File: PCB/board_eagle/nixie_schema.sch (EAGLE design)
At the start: 103 parts, among them J2 RTC_CONSMD, J4 RTC_CONTHT, P1 100k, Q1 BC856B, Q2 IRF740S, T1 PHOTO_TRANS, U2 MC7940N, Y1 ECS-.327-7-34B

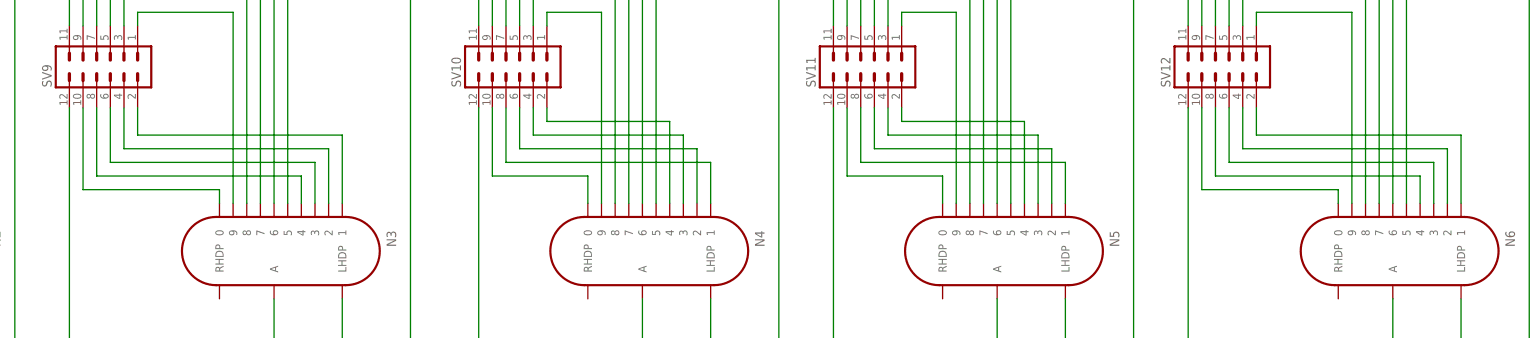
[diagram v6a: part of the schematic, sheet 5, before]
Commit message: Some more tob board routing
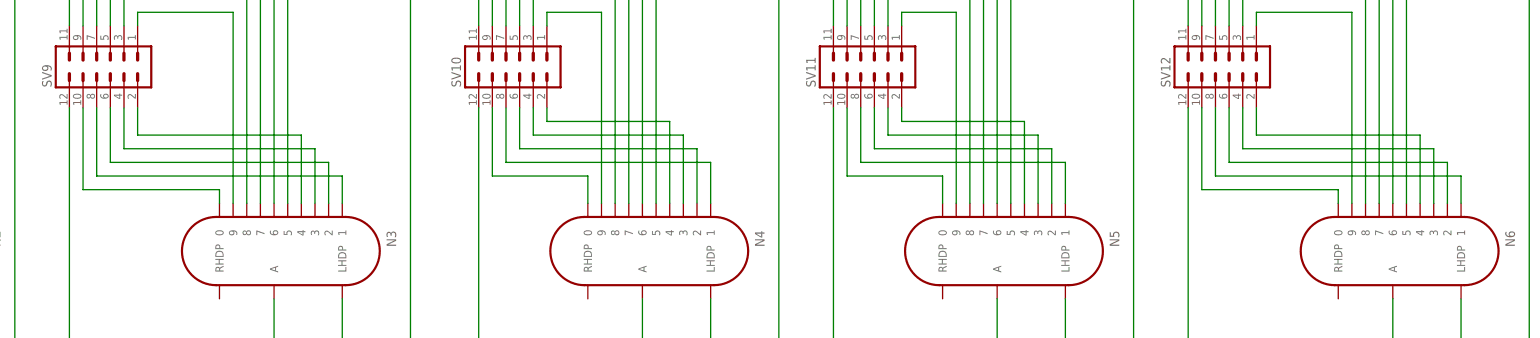
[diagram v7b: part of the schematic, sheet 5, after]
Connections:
- net N$52: now also N3.1; no longer N3.4
- net N$53: now also N3.2; no longer N3.3
- net N$54: now also N3.3; no longer N3.2
- net N$55: now also N3.4; no longer N3.1
- net N$81: now also N6.1; no longer N6.4
- net N$82: now also N6.2; no longer N6.3
- net N$83: now also N6.3; no longer N6.2
- net N$84: now also N6.4; no longer N6.1
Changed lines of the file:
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@@
 <net name="N$52" class="0">
 <segment>
+<pinref part="SV9" gate="1" pin="8"/>
+<wire x1="180.34" y1="25.4" x2="134.62" y2="25.4" width="0.1524" layer="91"/>
+<wire x1="134.62" y1="25.4" x2="134.62" y2="38.1" width="0.1524" layer="91"/>
+<pinref part="N3" gate="G$1" pin="1"/>
+<wire x1="180.34" y1="25.4" x2="180.34" y2="20.32" width="0.1524" layer="91"/>
+</segment>
+</net>
+<net name="N$53" class="0">
+<segment>
+<pinref part="SV9" gate="1" pin="6"/>
+<wire x1="137.16" y1="27.94" x2="137.16" y2="38.1" width="0.1524" layer="91"/>
+<pinref part="N3" gate="G$1" pin="2"/>
+<wire x1="137.16" y1="27.94" x2="177.8" y2="27.94" width="0.1524" layer="91"/>
+<wire x1="177.8" y1="27.94" x2="177.8" y2="20.32" width="0.1524" layer="91"/>
+</segment>
+</net>
+<net name="N$54" class="0">
+<segment>
+<pinref part="SV9" gate="1" pin="4"/>
+<wire x1="139.7" y1="30.48" x2="139.7" y2="38.1" width="0.1524" layer="91"/>
+<pinref part="N3" gate="G$1" pin="3"/>
+<wire x1="139.7" y1="30.48" x2="175.26" y2="30.48" width="0.1524" layer="91"/>
+<wire x1="175.26" y1="30.48" x2="175.26" y2="20.32" width="0.1524" layer="91"/>
+</segment>
+</net>
+<net name="N$55" class="0">
+<segment>
+<pinref part="SV9" gate="1" pin="2"/>
+<wire x1="142.24" y1="33.02" x2="142.24" y2="38.1" width="0.1524" layer="91"/>
 <pinref part="N3" gate="G$1" pin="4"/>
-<wire x1="172.72" y1="20.32" x2="172.72" y2="25.4" width="0.1524" layer="91"/>
-<pinref part="SV9" gate="1" pin="8"/>
-<wire x1="172.72" y1="25.4" x2="134.62" y2="25.4" width="0.1524" layer="91"/>
-<wire x1="134.62" y1="25.4" x2="134.62" y2="38.1" width="0.1524" layer="91"/>
-</segment>
-</net>
-<net name="N$53" class="0">
-<segment>
-<pinref part="N3" gate="G$1" pin="3"/>
-<wire x1="175.26" y1="20.32" x2="175.26" y2="27.94" width="0.1524" layer="91"/>
-<pinref part="SV9" gate="1" pin="6"/>
-<wire x1="175.26" y1="27.94" x2="137.16" y2="27.94" width="0.1524" layer="91"/>
-<wire x1="137.16" y1="27.94" x2="137.16" y2="38.1" width="0.1524" layer="91"/>
-</segment>
-</net>
-<net name="N$54" class="0">
-<segment>
-<pinref part="N3" gate="G$1" pin="2"/>
-<wire x1="177.8" y1="20.32" x2="177.8" y2="30.48" width="0.1524" layer="91"/>
-<pinref part="SV9" gate="1" pin="4"/>
-<wire x1="177.8" y1="30.48" x2="139.7" y2="30.48" width="0.1524" layer="91"/>
-<wire x1="139.7" y1="30.48" x2="139.7" y2="38.1" width="0.1524" layer="91"/>
-</segment>
-</net>
-<net name="N$55" class="0">
-<segment>
-<pinref part="N3" gate="G$1" pin="1"/>
-<wire x1="180.34" y1="20.32" x2="180.34" y2="33.02" width="0.1524" layer="91"/>
-<pinref part="SV9" gate="1" pin="2"/>
-<wire x1="180.34" y1="33.02" x2="142.24" y2="33.02" width="0.1524" layer="91"/>
-<wire x1="142.24" y1="33.02" x2="142.24" y2="38.1" width="0.1524" layer="91"/>
+<wire x1="142.24" y1="33.02" x2="172.72" y2="33.02" width="0.1524" layer="91"/>
+<wire x1="172.72" y1="33.02" x2="172.72" y2="20.32" width="0.1524" layer="91"/>
 </segment>
 </net>
@@
 <net name="N$81" class="0">
 <segment>
+<pinref part="SV12" gate="1" pin="8"/>
+<wire x1="388.62" y1="25.4" x2="342.9" y2="25.4" width="0.1524" layer="91"/>
+<wire x1="342.9" y1="25.4" x2="342.9" y2="38.1" width="0.1524" layer="91"/>
+<pinref part="N6" gate="G$1" pin="1"/>
+<wire x1="388.62" y1="25.4" x2="388.62" y2="20.32" width="0.1524" layer="91"/>
+</segment>
+</net>
+<net name="N$82" class="0">
+<segment>
+<pinref part="SV12" gate="1" pin="6"/>
+<wire x1="345.44" y1="27.94" x2="345.44" y2="38.1" width="0.1524" layer="91"/>
+<pinref part="N6" gate="G$1" pin="2"/>
+<wire x1="345.44" y1="27.94" x2="386.08" y2="27.94" width="0.1524" layer="91"/>
+<wire x1="386.08" y1="27.94" x2="386.08" y2="20.32" width="0.1524" layer="91"/>
+</segment>
+</net>
+<net name="N$83" class="0">
+<segment>
+<pinref part="SV12" gate="1" pin="4"/>
+<wire x1="347.98" y1="30.48" x2="347.98" y2="38.1" width="0.1524" layer="91"/>
+<pinref part="N6" gate="G$1" pin="3"/>
+<wire x1="347.98" y1="30.48" x2="383.54" y2="30.48" width="0.1524" layer="91"/>
+<wire x1="383.54" y1="30.48" x2="383.54" y2="20.32" width="0.1524" layer="91"/>
+</segment>
+</net>
+<net name="N$84" class="0">
+<segment>
+<pinref part="SV12" gate="1" pin="2"/>
+<wire x1="350.52" y1="33.02" x2="350.52" y2="38.1" width="0.1524" layer="91"/>
 <pinref part="N6" gate="G$1" pin="4"/>
-<wire x1="381" y1="20.32" x2="381" y2="25.4" width="0.1524" layer="91"/>
-<pinref part="SV12" gate="1" pin="8"/>
-<wire x1="381" y1="25.4" x2="342.9" y2="25.4" width="0.1524" layer="91"/>
-<wire x1="342.9" y1="25.4" x2="342.9" y2="38.1" width="0.1524" layer="91"/>
-</segment>
-</net>
-<net name="N$82" class="0">
-<segment>
-<pinref part="N6" gate="G$1" pin="3"/>
-<wire x1="383.54" y1="20.32" x2="383.54" y2="27.94" width="0.1524" layer="91"/>
-<pinref part="SV12" gate="1" pin="6"/>
-<wire x1="383.54" y1="27.94" x2="345.44" y2="27.94" width="0.1524" layer="91"/>
-<wire x1="345.44" y1="27.94" x2="345.44" y2="38.1" width="0.1524" layer="91"/>
-</segment>
-</net>
-<net name="N$83" class="0">
-<segment>
-<pinref part="N6" gate="G$1" pin="2"/>
-<wire x1="386.08" y1="20.32" x2="386.08" y2="30.48" width="0.1524" layer="91"/>
-<pinref part="SV12" gate="1" pin="4"/>
-<wire x1="386.08" y1="30.48" x2="347.98" y2="30.48" width="0.1524" layer="91"/>
-<wire x1="347.98" y1="30.48" x2="347.98" y2="38.1" width="0.1524" layer="91"/>
-</segment>
-</net>
-<net name="N$84" class="0">
-<segment>
-<pinref part="N6" gate="G$1" pin="1"/>
-<wire x1="388.62" y1="20.32" x2="388.62" y2="33.02" width="0.1524" layer="91"/>
-<pinref part="SV12" gate="1" pin="2"/>
-<wire x1="388.62" y1="33.02" x2="350.52" y2="33.02" width="0.1524" layer="91"/>
-<wire x1="350.52" y1="33.02" x2="350.52" y2="38.1" width="0.1524" layer="91"/>
-</segment>
-</net>
+<wire x1="350.52" y1="33.02" x2="381" y2="33.02" width="0.1524" layer="91"/>
+<wire x1="381" y1="33.02" x2="381" y2="20.32" width="0.1524" layer="91"/>
+</segment>
+</net>

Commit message: Started fixing nixie tube footprint
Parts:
- N1, N2, N3, N4, N5, N6: value IN-14 -> IN-14_FIXED; device russian-nixies:IN-14 -> russian-nixies:IN-14_FIXED
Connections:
- removed net N$101: N3.LHDP, SV9.11
- removed net N$102: N4.LHDP, SV10.11
- removed net N$104: N6.LHDP, SV12.11
- removed net N$105: N5.LHDP, SV11.11
- removed net N$31: N1.7, SV7.5
- removed net N$32: N1.8, SV7.3
- removed net N$33: N1.9, SV7.1
- removed net N$34: N2.9, SV8.1
- removed net N$35: N2.0, SV8.10
- removed net N$36: N2.1, SV8.8
- removed net N$37: N2.2, SV8.6
- removed net N$38: N2.3, SV8.4
- removed net N$39: N2.4, SV8.2
- removed net N$40: N2.5, SV8.9
- removed net N$41: N2.8, SV8.3
- removed net N$42: N2.7, SV8.5
- removed net N$43: N2.6, SV8.7
- removed net N$44: N4.1, SV10.8
- removed net N$46: N3.5, SV9.9
- removed net N$47: N3.6, SV9.7
- removed net N$48: N3.7, SV9.5
- removed net N$49: N3.8, SV9.3
- removed net N$50: N3.9, SV9.1
- removed net N$51: N3.0, SV9.10
- removed net N$52: N3.1, SV9.8
- removed net N$53: N3.2, SV9.6
- removed net N$54: N3.3, SV9.4
- removed net N$55: N3.4, SV9.2
- removed net N$56: N4.2, SV10.6
- removed net N$57: N4.3, SV10.4
- removed net N$58: N4.4, SV10.2
- removed net N$59: N4.5, SV10.9
- removed net N$60: N4.6, SV10.7
- removed net N$61: N4.7, SV10.5
- removed net N$62: N4.8, SV10.3
- removed net N$63: N4.9, SV10.1
- removed net N$64: N5.0, SV11.10
- removed net N$65: N5.1, SV11.8
- removed net N$66: N5.2, SV11.6
- removed net N$67: N5.3, SV11.4
- removed net N$68: N5.4, SV11.2
- removed net N$69: N5.5, SV11.9
- removed net N$70: N5.9, SV11.1
- removed net N$71: N5.8, SV11.3
- removed net N$72: N5.7, SV11.5
- removed net N$73: N5.6, SV11.7
- removed net N$75: N6.5, SV12.9
- removed net N$76: N6.6, SV12.7
- removed net N$77: N6.7, SV12.5
- removed net N$78: N6.8, SV12.3
- removed net N$79: N6.9, SV12.1
- removed net N$80: N6.0, SV12.10
- removed net N$81: N6.1, SV12.8
- removed net N$82: N6.2, SV12.6
- removed net N$83: N6.3, SV12.4
- removed net N$84: N6.4, SV12.2
- removed net N$86: N2.LHDP, SV8.11
- new net N$1: N2.RHDP, SV8.10
- new net N$2: N1.0, SV7.8
- new net N$6: N1.9, SV7.6
- new net N$7: N1.8, SV7.4
- net N$23: now also N3.RHDP, SV9.10; no longer N4.0, SV10.10
- net N$24: now also N1.7, SV7.2; no longer N1.0, SV7.10
- net N$25: now also SV7.9; no longer SV7.8
- net N$26: now also SV7.7; no longer SV7.6
- net N$27: now also SV7.5; no longer SV7.4
- net N$28: now also SV7.3; no longer SV7.2
- net N$29: now also SV7.1; no longer SV7.9
- net N$30: now also SV7.11; no longer SV7.7
- net N$94: now also N1.RHDP, SV7.10; no longer N1.LHDP, SV7.11
